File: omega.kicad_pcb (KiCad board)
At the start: 2 copper layers, 200 x 57.2 mm, 61 parts, among them SW1 SW_Push, U1 ProMicro

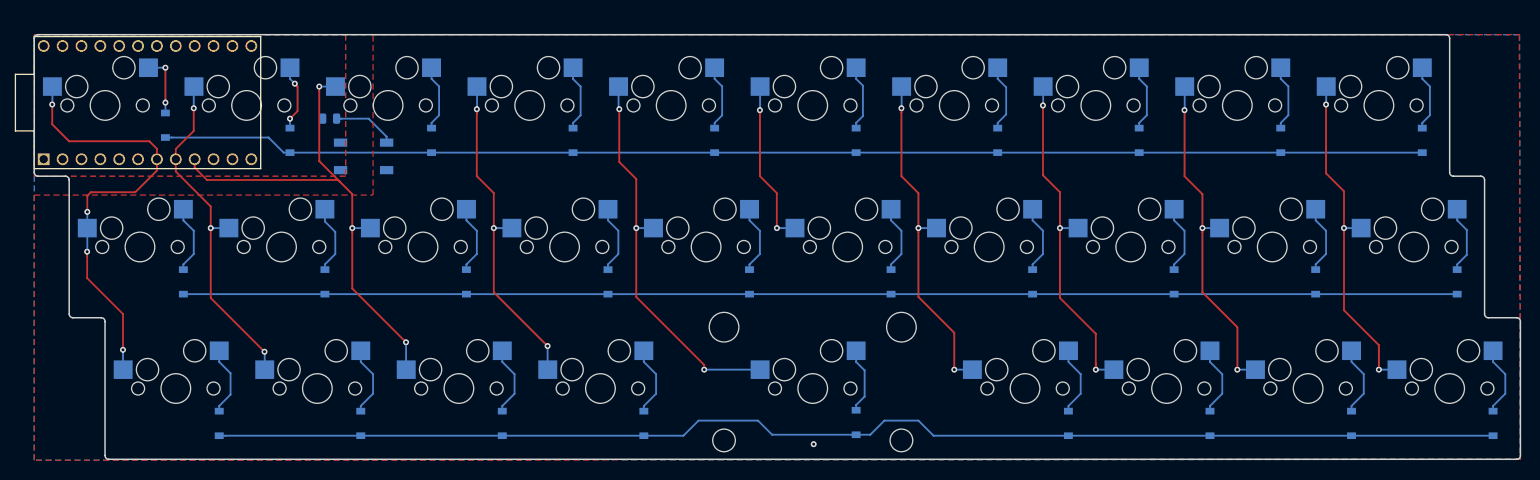
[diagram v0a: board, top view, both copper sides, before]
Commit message: flip pro micor and generate assembly files
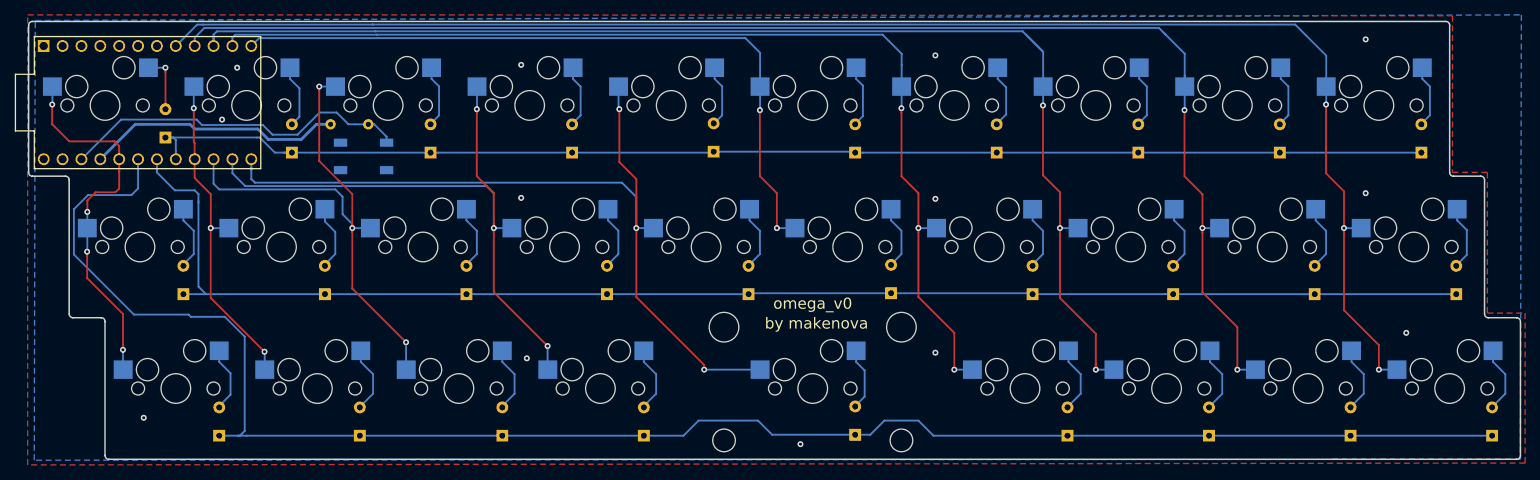
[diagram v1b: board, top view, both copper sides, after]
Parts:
- D1, D10, D11, D12, D13, D14, D15, D16, D17, D18, D19, D2, D20, D21, D22, D23, D24, D25, D26, D27, D28, D29, D3, D4, D5, D6, D7, D8, D9: footprint Diode_SMD:D_SOD-123 -> Diode_THT:D_DO-35_SOD27_P3.81mm_Vertical_AnodeUp
- R1: footprint Resistor_SMD:R_0805_2012Metric -> Resistor_THT:R_Axial_DIN0204_L3.6mm_D1.6mm_P5.08mm_Horizontal
- U1: moved to B.Cu
- moved D2 1.67 mm to (90.7, 57.3)
- moved D9 1.66 mm to (223.6, 57.3)
- moved D10 1.66 mm to (242.7, 57.3)
- moved D3 1.66 mm to (109.3, 57.3)
- moved D4 1.66 mm to (128.4, 57.3)
- moved D7 1.66 mm to (185.5, 57.3)
- moved D6 1.66 mm to (166.5, 57.3)
- moved D8 1.66 mm to (204.6, 57.3)
- moved D14 1.66 mm to (133.1, 76.3)
- moved D15 1.66 mm to (152.1, 76.3)
- moved D18 1.66 mm to (209.3, 76.3)
- moved D19 1.66 mm to (228.3, 76.3)
- moved D20 1.66 mm to (247.4, 76.3)
- moved D26 1.66 mm to (195.1, 95.4)
- moved D28 1.66 mm to (233.2, 95.4)
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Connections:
- U1 pad 10: Net-(U1-Pad10) -> COL7
- U1 pad 11: Net-(U1-Pad11) -> COL6
- U1 pad 12: Net-(U1-Pad12) -> COL5
- U1 pad 13: Net-(U1-Pad13) -> COL4
- U1 pad 14: Net-(U1-Pad14) -> COL3
- U1 pad 15: Net-(U1-Pad15) -> COL2
- U1 pad 16: Net-(U1-Pad16) -> COL1
- U1 pad 17: Net-(U1-Pad17) -> ROW0
- U1 pad 18: Net-(U1-Pad18) -> ROW1
- U1 pad 19: Net-(U1-Pad19) -> ROW2
- U1 pad 20: Net-(U1-Pad20) -> COL0
- U1 pad 7: COL0 -> Net-(U1-Pad7)
- U1 pad 8: COL1 -> COL9
- U1 pad 9: COL2 -> COL8
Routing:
- net COL9: track 45.8 -> 207.7 mm
- net COL8: track 45.8 -> 188.5 mm
- net COL7: track 46.7 -> 170.4 mm
- net COL6: track 45.9 -> 142.8 mm
- net COL5: track 22.4 -> 96.7 mm
- net ROW2: track 174.7 -> 236.0 mm
- net COL4: track 52.7 -> 112.6 mm
- net COL3: track 44.5 -> 87.4 mm
- net Net-(R1-Pad2): track 8.54 -> 47.5 mm
- net +5V: track 0.00 -> 34.1 mm
- net ROW1: track 171.4 -> 194.1 mm
- net COL0: track 59.7 -> 51.2 mm
- net COL2: track 69.0 -> 74.0 mm
- net ROW0: track 170.0 -> 175.0 mm
- net COL1: track 46.5 -> 44.5 mm
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- removed copper zone on F.Cu, net +5V
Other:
- board size 200 x 57.2 mm -> 200.8 x 58.9 mm
- net class Default: trace_width 0.25 -> 0.254
- net class Power added: clearance 0.2, trace_width 0.381, via_dia 0.8, via_drill 0.4
- board text added: "by makenova"
- board text added: "omega_v0"
